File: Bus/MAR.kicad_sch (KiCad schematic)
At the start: 2 parts, among them J6 Conn_01x10_Pin, J7 Conn_01x04_Pin

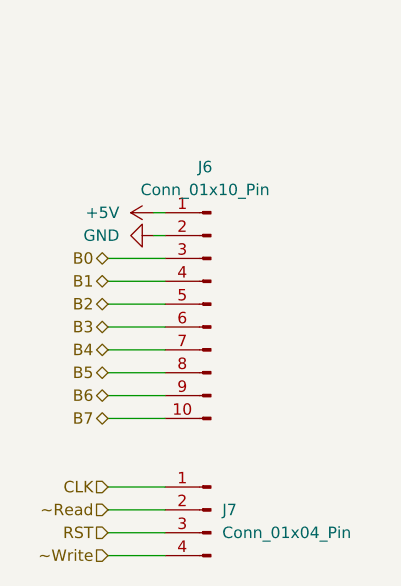
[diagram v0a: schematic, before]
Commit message: Updated bus schematics with pinout of MAR/ALU/Registers on PCBs ordered
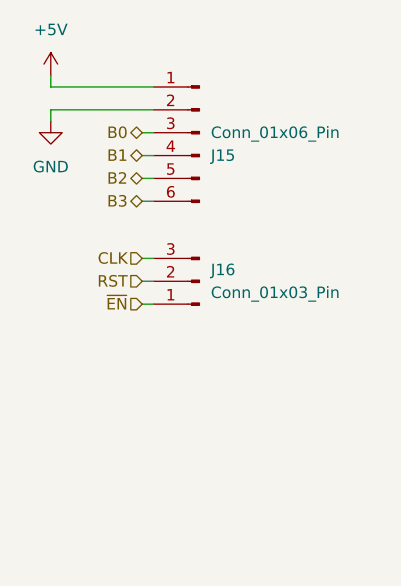
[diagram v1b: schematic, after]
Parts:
- removed J6: Conn_01x10_Pin, Connector_PinHeader_2.54mm:PinHeader_1x10_P2.54mm_Vertical, symbol Connector:Conn_01x10_Pin
- removed J7: Conn_01x04_Pin, Connector_PinHeader_2.54mm:PinHeader_1x04_P2.54mm_Vertical, symbol Connector:Conn_01x04_Pin
- added J15: Conn_01x06_Pin, Connector_PinHeader_2.54mm:PinHeader_1x06_P2.54mm_Vertical, symbol Connector:Conn_01x06_Pin
- added J16: Conn_01x03_Pin, Connector_PinHeader_2.54mm:PinHeader_1x03_P2.54mm_Vertical, symbol Connector:Conn_01x03_Pin
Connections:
- net +5V: now also J15.1 (Pin_1)
- net B0: now also J15.3 (Pin_3)
- net B1: now also J15.4 (Pin_4)
- net B2: now also J15.5 (Pin_5)
- net B3: now also J15.6 (Pin_6)
- net CLK: now also J16.3 (Pin_3)
- net GND: now also J15.2 (Pin_2)
- net RST: now also J16.2 (Pin_2)
- new net ~{EN}: J16.1 (Pin_1)
